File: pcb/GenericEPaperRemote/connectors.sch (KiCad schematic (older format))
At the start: 32 parts, among them J5 Barrel_Jack, Q1 BC817, Q2 BC817, U2 FT232RL, U3 NCP1117ST33T3G

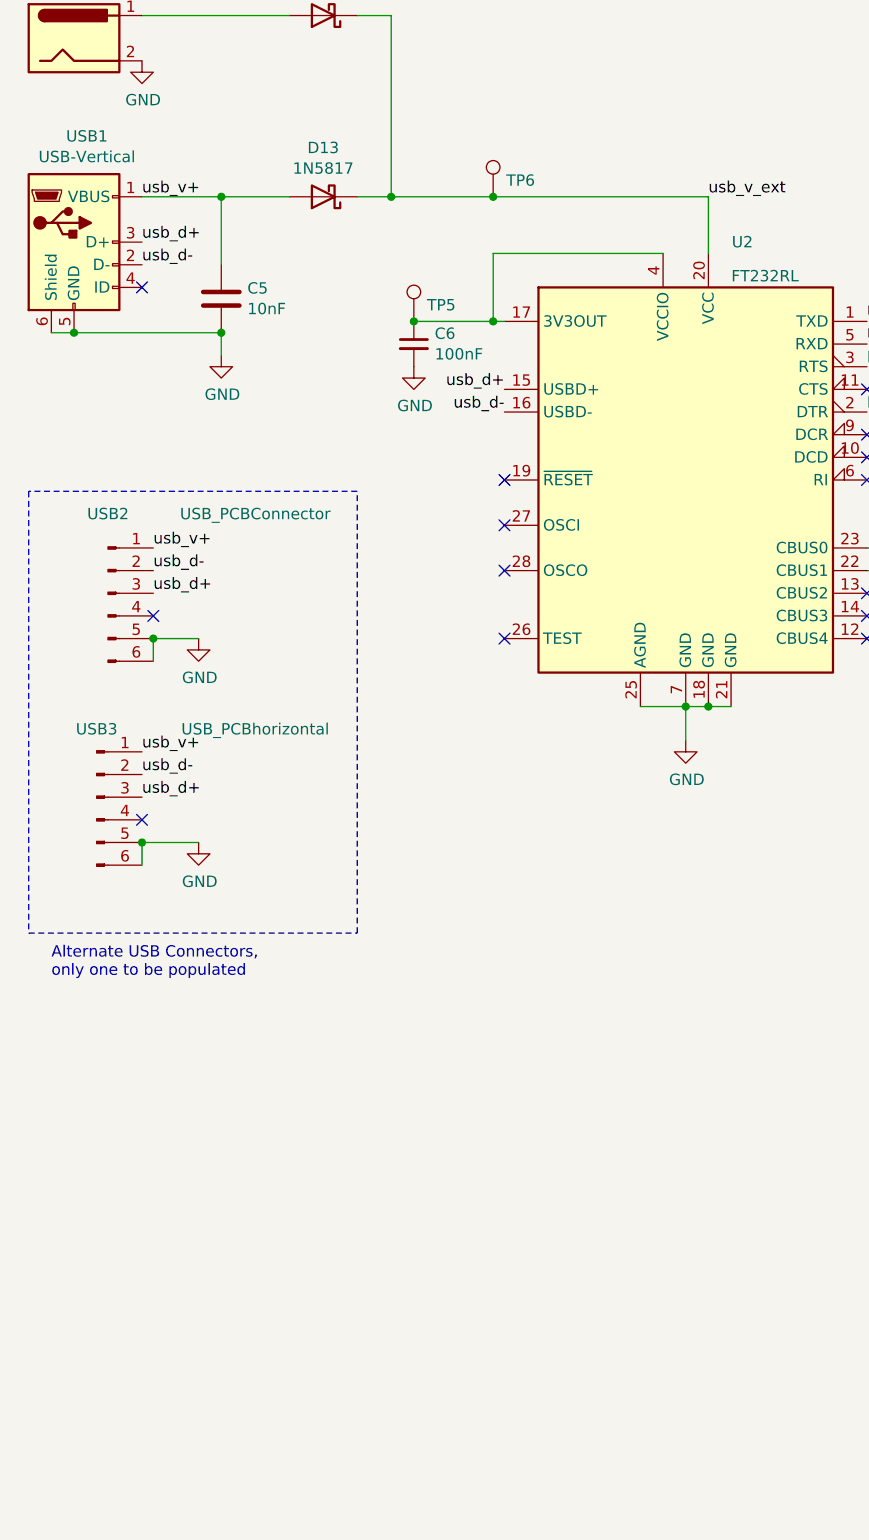
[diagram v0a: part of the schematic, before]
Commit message: Added pullups for encoder and switch away from io0 to prevent boot to root-loader when rotary encoder pulls low)
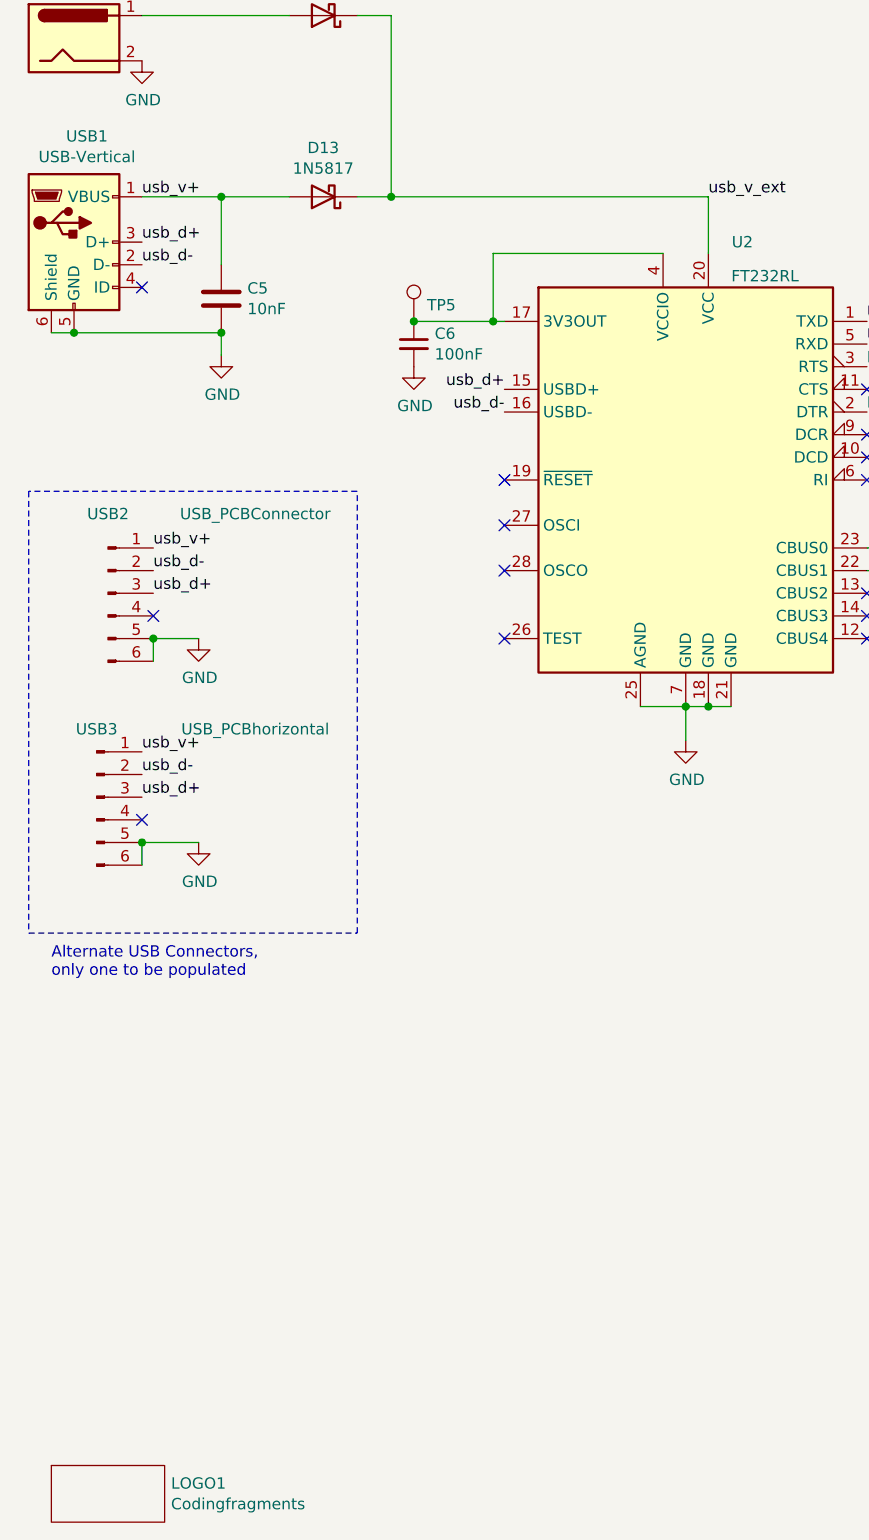
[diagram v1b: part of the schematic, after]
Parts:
- removed TP6: TestPoint, TestPoint:TestPoint_THTPad_2.0x2.0mm_Drill1.0mm, symbol Connector:TestPoint
- added LOGO1: Codingfragments, codingfragment-components:OSSLogo, symbol GenericEPaperRemote-rescue:OSS-logo-Codingfragments_common
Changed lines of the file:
@@
 $EndComp
-$Comp
-L Connector:TestPoint TP6
-U 1 1 5F6B303B
-P 2850 1600
-F 0 "TP6" H 2908 1672 50  0000 L CNN
-F 1 "TestPoint" H 2908 1627 50  0001 L CNN
-F 2 "TestPoint:TestPoint_THTPad_2.0x2.0mm_Drill1.0mm" H 3050 1600 50  0001 C CNN
-F 3 "~" H 3050 1600 50  0001 C CNN
-	1    2850 1600
-	1    0    0    -1
-$EndComp
-Connection ~ 2850 1600
-Wire Wire Line
-	2850 1600 3800 1600
 $Comp
 L Connector:TestPoint TP5
@@
 Connection ~ 2400 1600
 Wire Wire Line
-	2400 1600 2850 1600
-Wire Wire Line
 	1350 3650 1350 3550
 Wire Wire Line
@@
 NoConn ~ 1300 4350
 NoConn ~ 1350 3450
+Wire Wire Line
+	2400 1600 3800 1600
+$Comp
+L GenericEPaperRemote-rescue:OSS-logo-Codingfragments_common LOGO1
+U 1 1 5FAE0DC1
+P 1150 7350
+F 0 "LOGO1" H 1428 7421 50  0000 L CNN
+F 1 "Codingfragments" H 1428 7330 50  0000 L CNN
+F 2 "codingfragment-components:OSSLogo" H 1150 7350 50  0001 C CNN
+F 3 "" H 1150 7350 50  0001 C CNN
+	1    1150 7350
+	1    0    0    -1
+$EndComp
 $EndSCHEMATC
